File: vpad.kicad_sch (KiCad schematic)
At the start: 53 parts, among them J1 Conn_01x10_Socket, J2 Conn_01x10_Socket, SW1 SW_Push_45deg, SW10 SW_Push_45deg, SW11 SW_Push_45deg, SW12 SW_Push_45deg, SW13 SW_Push_45deg, SW14 SW_Push_45deg, SW15 SW_Push_45deg, SW16 SW_Push_45deg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

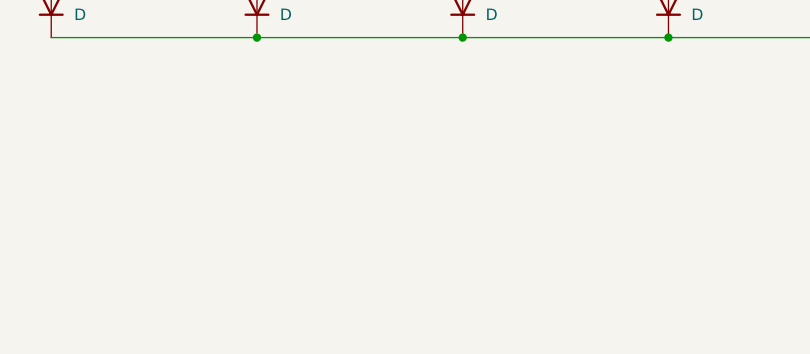
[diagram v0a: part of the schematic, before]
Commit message: added mounting holes
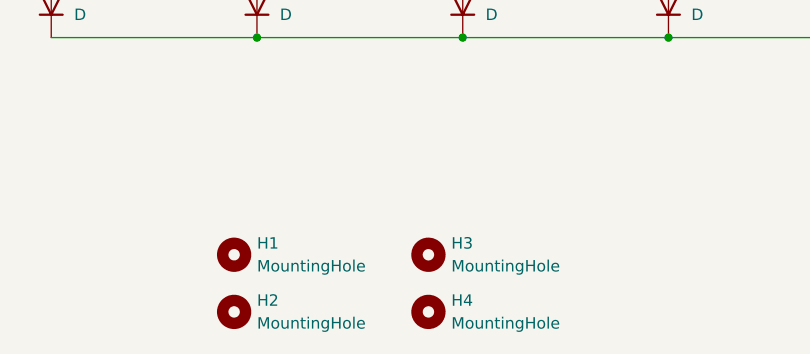
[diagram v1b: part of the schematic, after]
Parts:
- added H1, H2, H3, H4: MountingHole, MountingHole:MountingHole_2.2mm_M2, symbol Mechanical:MountingHole

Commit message: edited mounting to m3, added case
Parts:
- H1, H2, H3, H4: footprint MountingHole:MountingHole_2.2mm_M2 -> MountingHole:MountingHole_3.2mm_M3
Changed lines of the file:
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@@
 			)
 		)
-		(property "Footprint" "MountingHole:MountingHole_2.2mm_M2"
+		(property "Footprint" "MountingHole:MountingHole_3.2mm_M3"
 			(at 124.46 161.29 0)
 			(effects
@@
 			)
 		)
-		(property "Footprint" "MountingHole:MountingHole_2.2mm_M2"
+		(property "Footprint" "MountingHole:MountingHole_3.2mm_M3"
 			(at 102.87 161.29 0)
 			(effects
@@
 			)
 		)
-		(property "Footprint" "MountingHole:MountingHole_2.2mm_M2"
+		(property "Footprint" "MountingHole:MountingHole_3.2mm_M3"
 			(at 124.46 167.64 0)
 			(effects
@@
 			)
 		)
-		(property "Footprint" "MountingHole:MountingHole_2.2mm_M2"
+		(property "Footprint" "MountingHole:MountingHole_3.2mm_M3"
 			(at 102.87 167.64 0)
 			(effects
